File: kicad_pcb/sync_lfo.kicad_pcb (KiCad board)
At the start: 2 copper layers, 30 x 110 mm, 23 parts, among them J1 CLOCK IN, J2 OUT, J3 Connector 2x8

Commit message: feat: :sparkles: rev 0.2 pcb and schematics
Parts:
- added R8: R 33K, Resistor_THT:R_Axial_DIN0204_L3.6mm_D1.6mm_P2.54mm_Vertical, B.Cu at (23.0, 67.4)
- C1, C2, C3, C4: value C -> C 220pF; footprint Capacitor_THT:C_Disc_D3.0mm_W1.6mm_P2.50mm -> Capacitor_THT:C_Disc_D4.3mm_W1.9mm_P5.00mm
- C5: value C -> C 4.7 µF
- R1, R4, R5, R6, R7: value R -> R 470
- R2: value R -> R 1K
- R3: value R -> R 100K
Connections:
- D3 pad 2: Net-(A1-D10) -> Net-(D3-A)
- J3 pad 10: +12V -> GND
- J3 pad 11: unconnected-(J3-Pin_11-Pad11) -> GND
- J3 pad 12: unconnected-(J3-Pin_12-Pad12) -> GND
- J3 pad 13: unconnected-(J3-Pin_13-Pad13) -> GND
- J3 pad 14: unconnected-(J3-Pin_14-Pad14) -> GND
- J3 pad 3: GND -> unconnected-(J3-Pin_3-Pad3)
- J3 pad 4: GND -> unconnected-(J3-Pin_4-Pad4)
- J3 pad 5: GND -> unconnected-(J3-Pin_5-Pad5)
- J3 pad 6: GND -> unconnected-(J3-Pin_6-Pad6)
- J3 pad 7: GND -> +12V
- J3 pad 8: GND -> +12V
- J3 pad 9: +12V -> GND
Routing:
- net Net-(D3-A): track 0.00 -> 48.8 mm
- net Net-(R4-Pad1): track 19.9 -> 67.8 mm
- net GND: track 181.0 -> 194.0 mm
- net Net-(A1-D3): track 76.2 -> 86.2 mm
- net +5V: track 87.7 -> 97.0 mm
- net Net-(R1-Pad1): track 17.8 -> 23.2 mm
- net Net-(R5-Pad1): track 16.7 -> 20.7 mm
- net Net-(A1-D10): track 91.7 -> 89.1 mm
- net +12V: track 30.5 -> 32.4 mm
- net Net-(C5-Pad2): track 21.5 -> 22.7 mm
- net Net-(A1-A5): track 55.2 -> 56.4 mm
- net Net-(A1-A1): track 19.5 -> 20.6 mm
- net Net-(A1-A3): track 36.6 -> 36.5 mm, vias 0 -> 1
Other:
- board text added: "rev 0.2"
- board text removed: "rev 0.1"

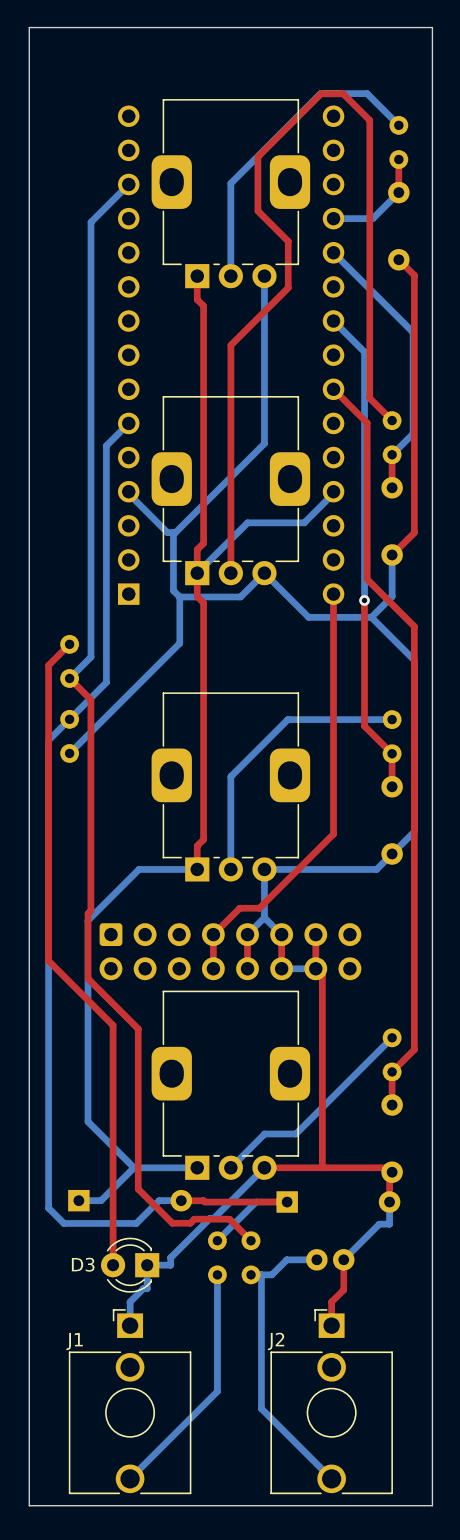
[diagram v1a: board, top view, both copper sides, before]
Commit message: feat: :sparkles: 10pin connector, drill holes, for distance, better routing
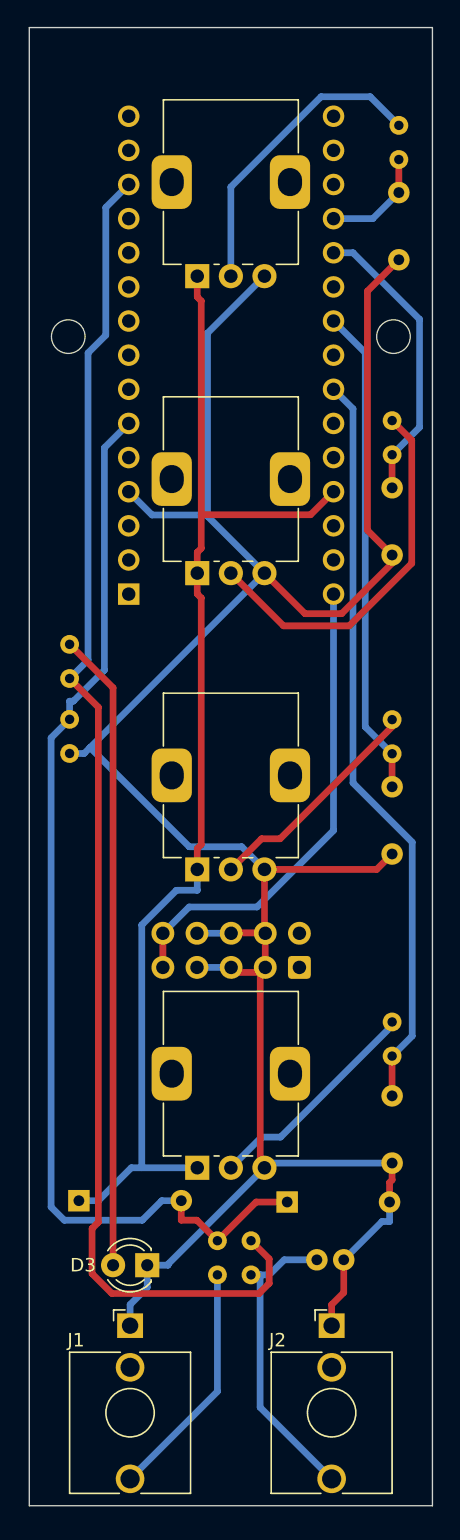
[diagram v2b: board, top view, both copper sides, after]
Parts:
- added HOLE RIGHT: MountingHole_2.5mm, MountingHole:MountingHole_2.5mm, B.Cu at (47.1, 42.0)
- added REF**: MountingHole_2.5mm, MountingHole:MountingHole_2.5mm, B.Cu at (22.9, 42.0)
- J3: value Connector 2x8 -> Connector_02x05; footprint Connector_IDC:IDC-Header_2x08_P2.54mm_Vertical -> Connector_IDC:IDC-Header_2x05_P2.54mm_Vertical
- moved J3 14.2 mm to (40.1, 88.9), turned to 90 degrees
- moved R6 1.18 mm to (47.0, 93.0)
- moved C4 0.68 mm to (47.0, 98.5)
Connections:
- J3 pad 10: GND -> +12V
- J3 pad 3: unconnected-(J3-Pin_3-Pad3) -> GND
- J3 pad 4: unconnected-(J3-Pin_4-Pad4) -> GND
- J3 pad 5: unconnected-(J3-Pin_5-Pad5) -> GND
- J3 pad 6: unconnected-(J3-Pin_6-Pad6) -> GND
- J3 pad 7: +12V -> GND
- J3 pad 8: +12V -> GND
- J3 pad 9: GND -> +12V
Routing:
- net Net-(R4-Pad1): track 67.8 -> 28.2 mm
- net Net-(A1-D10): track 89.1 -> 101.8 mm
- net +5V: track 97.0 -> 89.8 mm
- net GND: track 194.0 -> 188.7 mm
- net Net-(R5-Pad1): track 20.7 -> 16.9 mm
- net +12V: track 32.4 -> 36.0 mm
- net Net-(A1-D3): track 86.2 -> 82.7 mm
- net Net-(D3-A): track 48.8 -> 47.5 mm
- net Net-(A1-A1): track 20.6 -> 21.8 mm
- net Net-(A1-A5): track 56.4 -> 55.6 mm
- net Net-(R6-Pad1): track 16.0 -> 16.7 mm
- net Net-(A1-A3): vias 1 -> 0

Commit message: feat: :lipstick: update design files, overall design system, clean placement file
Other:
- board text added: "schematics & code by HAGIWO modifications, design & pcb by l-i-l.de"

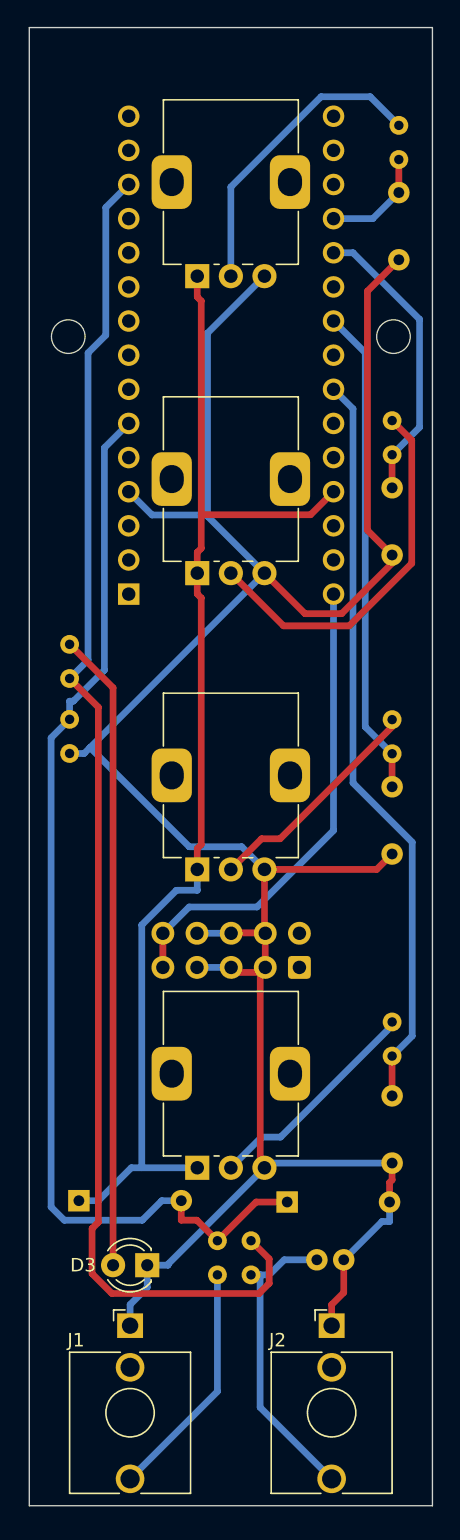
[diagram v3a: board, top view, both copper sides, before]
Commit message: feat: :sparkles: inv output, new design, reposition
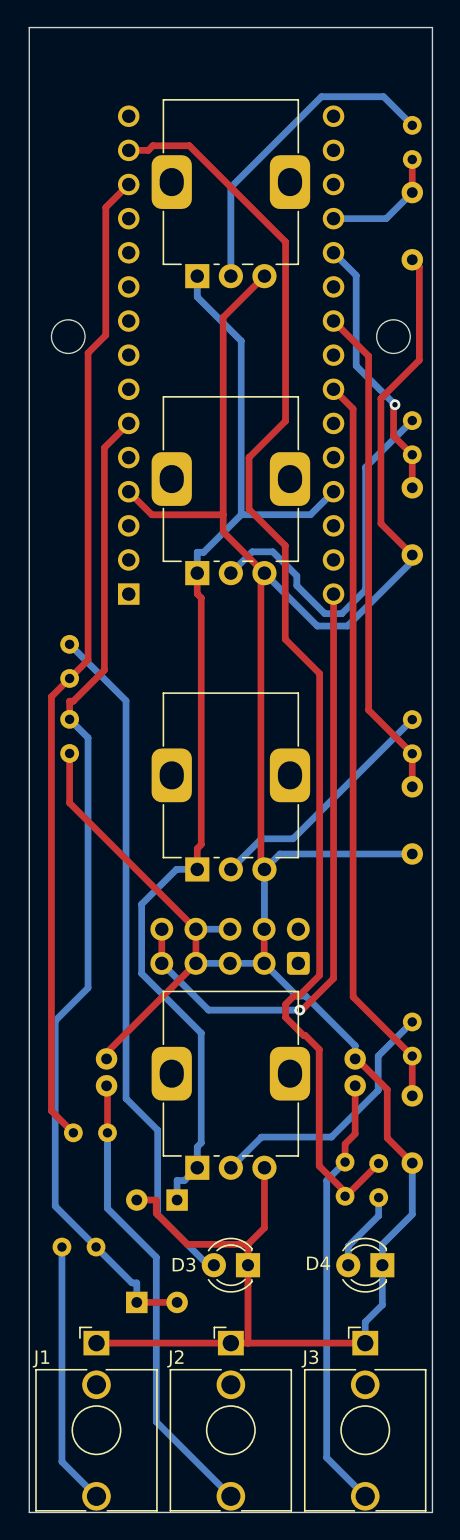
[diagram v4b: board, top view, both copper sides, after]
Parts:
- added C6: C 4.7 µF, Capacitor_THT:C_Radial_D5.0mm_H11.0mm_P2.00mm, B.Cu at (44.2, 95.8)
- added D4: LED, LED_THT:LED_D3.0mm, F.Cu at (46.3, 111.1)
- added J4: Connector_02x05, Connector_IDC:IDC-Header_2x05_P2.54mm_Vertical, B.Cu at (40.0, 88.6)
- added R10: R 470, Resistor_THT:R_Axial_DIN0204_L3.6mm_D1.6mm_P2.54mm_Vertical, B.Cu at (43.5, 106.0)
- added R9: R 33K, Resistor_THT:R_Axial_DIN0204_L3.6mm_D1.6mm_P2.54mm_Vertical, B.Cu at (46.0, 103.5)
- J3: value Connector_02x05 -> INV; footprint Connector_IDC:IDC-Header_2x05_P2.54mm_Vertical -> Connector_Audio:Jack_3.5mm_QingPu_WQP-PJ398SM_Vertical_CircularHoles; moved to F.Cu
- moved J3 28.4 mm to (45.0, 116.9), turned to 0 degrees
- moved C5 23.1 mm to (25.8, 95.8), turned to -90 degrees
- moved R7 15.5 mm to (23.3, 101.2), turned to 0 degrees
- moved D1 13.5 mm to (28.0, 113.9), turned to 90 degrees
- moved R2 9.04 mm to (25.0, 109.8), turned to 180 degrees
- moved J2 7.61 mm to (35.0, 116.9)
- moved D3 7.50 mm to (36.3, 111.1)
- moved D2 7.31 mm to (31.0, 106.2), turned to -90 degrees
- moved J1 2.82 mm to (25.0, 116.9)
- moved C2 1.50 mm to (48.5, 53.2)
- moved C3 1.50 mm to (48.5, 75.5)
- moved C4 1.50 mm to (48.5, 98.5)
- moved R4 1.50 mm to (48.5, 48.2)
- moved R5 1.50 mm to (48.5, 70.5)
- moved R6 1.50 mm to (48.5, 93.0)
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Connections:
- A1 pad 14: unconnected-(A1-D11-Pad14) -> Net-(A1-D11)
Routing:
- net Net-(A1-D11): track 0.00 -> 95.7 mm
- net GND: track 188.7 -> 228.1 mm
- net Net-(C6-Pad2): track 0.00 -> 32.6 mm
- net Net-(A1-D10): track 101.8 -> 73.6 mm
- net Net-(C5-Pad2): track 22.7 -> 34.4 mm
- net +12V: track 36.0 -> 46.3 mm, vias 0 -> 1
- net Net-(A1-D3): track 82.7 -> 74.7 mm
- net Net-(D4-A): track 0.00 -> 5.97 mm
- net +5V: track 89.8 -> 85.1 mm
- net Net-(D3-A): track 47.5 -> 50.9 mm
- net Net-(R6-Pad1): track 16.7 -> 19.5 mm
- net Net-(A1-A1): track 21.8 -> 20.0 mm, vias 0 -> 1
- net Net-(J1-PadT): track 17.9 -> 19.6 mm
- net Net-(R5-Pad1): track 16.9 -> 18.1 mm
- net Net-(A1-A0): track 8.12 -> 9.12 mm
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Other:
- board size 30 x 110 mm -> 30 x 110.5 mm
